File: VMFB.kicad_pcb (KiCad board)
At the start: 2 copper layers, 154.1 x 111.9 mm, 137 parts, among them J1 Screw_Terminal_01x02, J10 Conn_01x03_Pin, J11 Conn_01x08_Pin, J12 Conn_01x06_Pin, J13 Conn_01x03_Pin, J14 Conn_01x03_Pin, J15 Conn_01x03_Pin, J16 Conn_01x03_Pin, J17 Conn_01x03_Pin, J18 Conn_01x03_Pin, J19 Conn_01x02_Pin, J2 USB_A_Stacked, J20 Conn_01x03_Pin, J21 Conn_01x02_Pin, J3 USB_B, J4 Barrel_Jack_Switch, J5 Conn_01x02_Pin, J6 Conn_01x03_Pin, J7 Conn_01x02_Pin, J8 Conn_01x03_Pin, J9 Conn_01x03_Pin, Q1 BC547B, Q2 TIP41C, Q3 BC547B, Q4 BC547B, Q5 BD139, Q6 BC547B, Q7 BC547B, Q8 BC547, U1 NE555P, U2 NE555P, U3 LM358, U4 NE555P, U5 NE555P

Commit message: schemati and pcb tweaking
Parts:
- moved J21 1.52 mm to (217.9, 133.1)
- moved C11 0.48 mm to (162.7, 48.4)
- moved D6 0.48 mm to (183.0, 61.8)
- moved R28 0.48 mm to (177.7, 61.2)
- moved R31 0.48 mm to (182.8, 42.8)
- moved R32 0.48 mm to (187.6, 50.0)
- moved R33 0.48 mm to (186.5, 57.1)
- moved U5 0.48 mm to (182.6, 48.3)
- moved Q6 0.48 mm to (180.2, 65.6)
- moved R23 0.48 mm to (169.5, 68.8)
- moved C13 0.48 mm to (174.9, 59.7)
- moved D4 0.48 mm to (172.1, 45.3)
- moved D7 0.48 mm to (188.4, 45.3)
- moved R27 0.48 mm to (177.5, 42.8)
- moved C14 0.48 mm to (185.8, 66.6)
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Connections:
- J18 pad 2: GND -> IR GND
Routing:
- net IR GND: track 145.5 -> 178.0 mm
- net Net-(D1-K): track 153.8 -> 138.2 mm
- net IR CON/MON: track 100.8 -> 115.0 mm
- net EMPTY MON: track 87.1 -> 100.3 mm
- net DISPENSE CON/MON: track 69.8 -> 59.5 mm, vias 0 -> 1
- net Net-(J17-Pin_1): track 67.6 -> 58.3 mm
- net VCC: track 407.2 -> 416.5 mm
- net PIR MON: track 162.2 -> 154.7 mm
- net Net-(Q2-B): track 24.7 -> 18.9 mm
- net Net-(J8-Pin_1): track 129.8 -> 134.3 mm
- net DISPENSE ADJ: track 16.5 -> 13.6 mm
- net Net-(IR3-A): track 60.8 -> 63.6 mm
- net MOTOR RESET: track 173.4 -> 175.5 mm
- net Net-(J13-Pin_2): track 51.3 -> 49.4 mm
- net GND: track 535.9 -> 534.0 mm
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
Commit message: schemati and pcb tweaking
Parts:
- renumbered J7 to J6, J6 to J7, Q2 to Q1, Q1 to Q2, R11 to R10, R9 to R11, R25 to R23, R23 to R25, R30 to R29, R29 to R30, R33 to R32, R32 to R33, R5 to R4, R4 to R5, R7 to R6, R6 to R7, R10 to R8, R8 to R9
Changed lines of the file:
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@@
     (property "ki_keywords" "connector")
     (attr through_hole)
-    (fp_text reference "J6" (at 0 -2.33 -90) (layer "F.SilkS")
+    (fp_text reference "J7" (at 0 -2.33 -90) (layer "F.SilkS")
         (effects (font (size 1 1) (thickness 0.15)))
     )
@@
     (property "ki_keywords" "R res resistor")
     (attr through_hole)
-    (fp_text reference "R10" (at 1.27 -2.37 90) (layer "F.SilkS")
+    (fp_text reference "R8" (at 1.27 -2.37 90) (layer "F.SilkS")
         (effects (font (size 1 1) (thickness 0.15)))
     )
@@
     (property "ki_keywords" "power NPN Transistor")
     (attr through_hole)
-    (fp_text reference "Q2" (at 2.54 -4.27 90) (layer "F.SilkS")
+    (fp_text reference "Q1" (at 2.54 -4.27 90) (layer "F.SilkS")
         (effects (font (size 1 1) (thickness 0.15)))
     )
@@
     (property "ki_keywords" "R res resistor")
     (attr through_hole)
-    (fp_text reference "R30" (at 4.4698 -0.0612 90) (layer "F.SilkS")
+    (fp_text reference "R29" (at 4.4698 -0.0612 90) (layer "F.SilkS")
         (effects (font (size 1 1) (thickness 0.15)))
     )
@@
     (property "ki_keywords" "R res resistor")
     (attr through_hole)
-    (fp_text reference "R23" (at 1.299 2.54) (layer "F.SilkS")
+    (fp_text reference "R25" (at 1.299 2.54) (layer "F.SilkS")
         (effects (font (size 1 1) (thickness 0.15)))
     )
@@
     (property "ki_keywords" "R res resistor")
     (attr through_hole)
-    (fp_text reference "R25" (at 1.27 -2.72 -90) (layer "F.SilkS")
+    (fp_text reference "R23" (at 1.27 -2.72 -90) (layer "F.SilkS")
         (effects (font (size 1 1) (thickness 0.15)))
     )
@@
     (property "ki_keywords" "connector")
     (attr through_hole)
-    (fp_text reference "J7" (at 0 -2.33) (layer "F.SilkS")
+    (fp_text reference "J6" (at 0 -2.33) (layer "F.SilkS")
         (effects (font (size 1 1) (thickness 0.15)))
     )
@@
     (property "ki_keywords" "R res resistor")
     (attr through_hole)
-    (fp_text reference "R29" (at 4.2164 -0.0254) (layer "F.SilkS")
+    (fp_text reference "R30" (at 4.2164 -0.0254) (layer "F.SilkS")
         (effects (font (size 1 1) (thickness 0.15)))
     )
@@
     (property "ki_keywords" "NPN Transistor")
     (attr through_hole)
-    (fp_text reference "Q1" (at 2.54 -3.56 -90) (layer "F.SilkS")
+    (fp_text reference "Q2" (at 2.54 -3.56 -90) (layer "F.SilkS")
         (effects (font (size 1 1) (thickness 0.15)))
     )
@@
     (property "ki_keywords" "R res resistor")
     (attr through_hole)
-    (fp_text reference "R33" (at 1.27 2.54 90) (layer "F.SilkS")
+    (fp_text reference "R32" (at 1.27 2.54 90) (layer "F.SilkS")
         (effects (font (size 1 1) (thickness 0.15)))
     )
@@
     (property "ki_keywords" "R res resistor")
     (attr through_hole)
-    (fp_text reference "R9" (at 1.27 -2.37 90) (layer "F.SilkS")
+    (fp_text reference "R11" (at 1.27 -2.37 90) (layer "F.SilkS")
         (effects (font (size 1 1) (thickness 0.15)))
     )
@@
     (property "ki_keywords" "R res resistor")
     (attr through_hole)
-    (fp_text reference "R4" (at 1.27 -2.37 90) (layer "F.SilkS")
+    (fp_text reference "R5" (at 1.27 -2.37 90) (layer "F.SilkS")
         (effects (font (size 1 1) (thickness 0.15)))
     )
@@
     (property "ki_keywords" "R res resistor")
     (attr through_hole)
-    (fp_text reference "R5" (at 1.27 -2.37 90) (layer "F.SilkS")
+    (fp_text reference "R4" (at 1.27 -2.37 90) (layer "F.SilkS")
         (effects (font (size 1 1) (thickness 0.15)))
     )
@@
     (property "ki_keywords" "R res resistor")
     (attr through_hole)
-    (fp_text reference "R32" (at 1.328 2.54) (layer "F.SilkS")
+    (fp_text reference "R33" (at 1.328 2.54) (layer "F.SilkS")
         (effects (font (size 1 1) (thickness 0.15)))
     )
@@
     (property "ki_keywords" "R res resistor")
     (attr through_hole)
-    (fp_text reference "R11" (at 1.27 -2.37 90) (layer "F.SilkS")
+    (fp_text reference "R10" (at 1.27 -2.37 90) (layer "F.SilkS")
         (effects (font (size 1 1) (thickness 0.15)))
     )
@@
     (property "ki_keywords" "R res resistor")
     (attr through_hole)
-    (fp_text reference "R8" (at 4.709 0.0826 90) (layer "F.SilkS")
+    (fp_text reference "R9" (at 4.709 0.0826 90) (layer "F.SilkS")
         (effects (font (size 1 1) (thickness 0.15)))
     )
@@
     (property "ki_keywords" "R res resistor")
     (attr through_hole)
-    (fp_text reference "R6" (at 1.27 -2.72 90) (layer "F.SilkS")
+    (fp_text reference "R7" (at 1.27 -2.72 90) (layer "F.SilkS")
         (effects (font (size 1 1) (thickness 0.15)))
     )
@@
     (property "ki_keywords" "R res resistor")
     (attr through_hole)
-    (fp_text reference "R7" (at 1.27 -2.72 90) (layer "F.SilkS")
+    (fp_text reference "R6" (at 1.27 -2.72 90) (layer "F.SilkS")
         (effects (font (size 1 1) (thickness 0.15)))
     )
@@
       (xy 90.17 76.708)
       (xy 90.17 53.34)
-      (xy 93.98 53.086)
-      (xy 98.298 58.42)
+      (xy 93.726 52.07)
+      (xy 98.298 60.96)
       (xy 98.293338 77.560157)
     )
@@
       (xy 96.012 39.624)
       (xy 96.012 47.752)
-      (xy 93.98 53.086)
+      (xy 93.726 52.07)
     )
     (stroke (width 0.1) (type solid)) (fill none) (layer "F.SilkS"))
@@
       (xy 96.012 39.624)
       (xy 96.012 47.752)
-      (xy 93.98 53.086)
-      (xy 98.298 58.42)
+      (xy 93.726 52.07)
+      (xy 98.298 60.96)
       (xy 98.293338 77.560157)
       (xy 126.492 80.518)

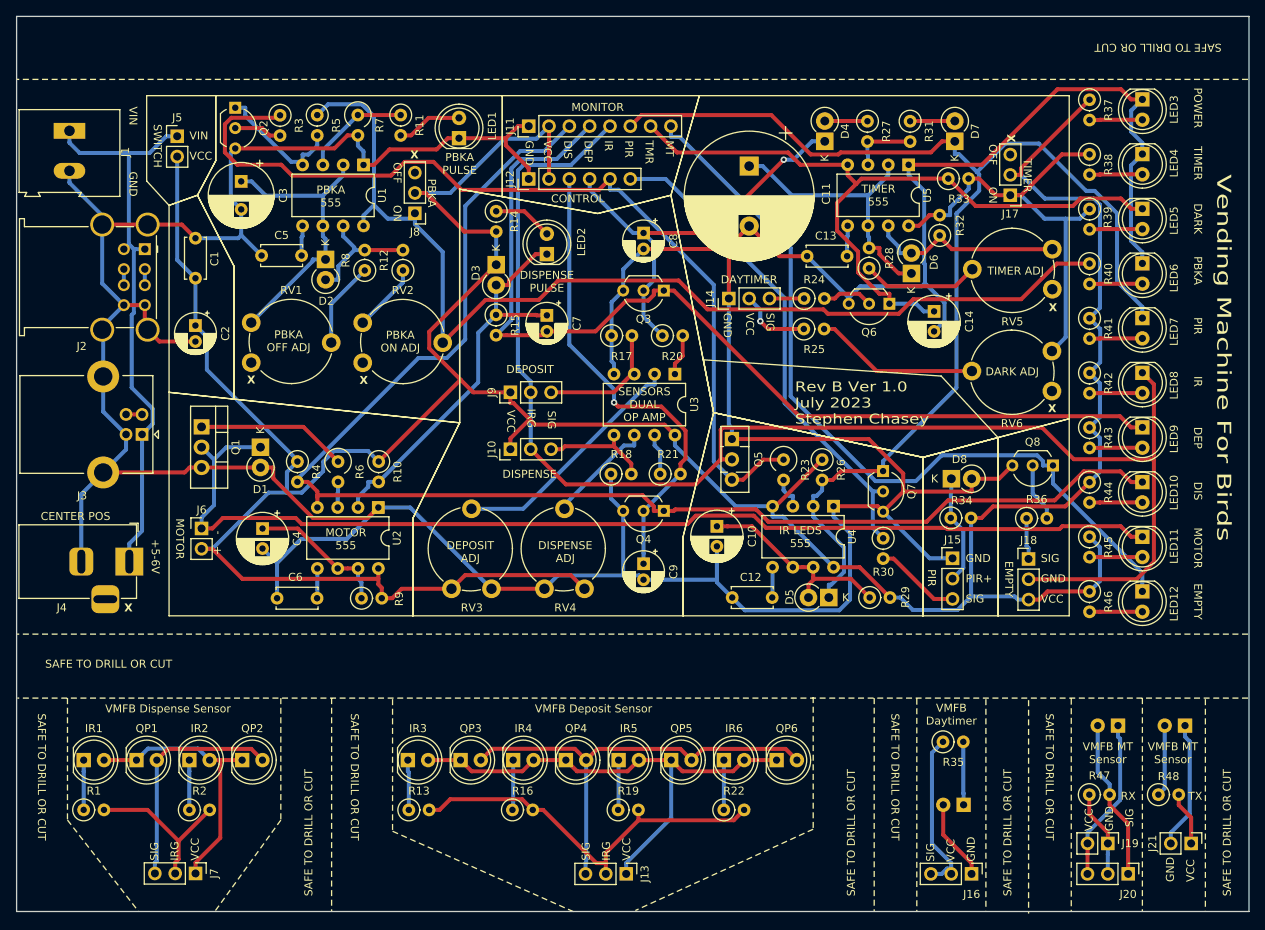
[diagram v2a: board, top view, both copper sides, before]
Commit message: schematic and pcb tweaking
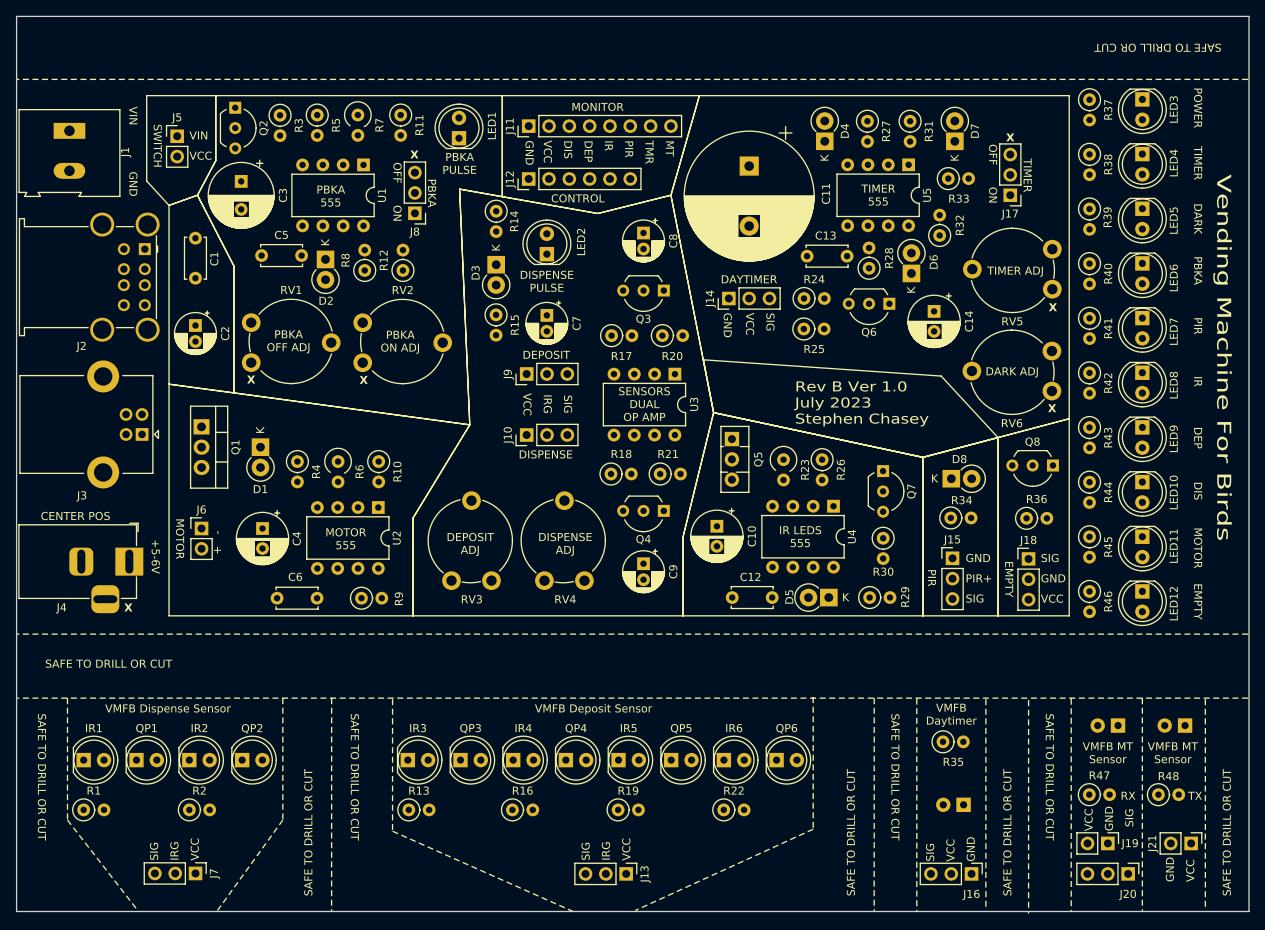
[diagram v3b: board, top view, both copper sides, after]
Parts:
- R33: value 47K -> 10K
- moved J9 3.06 mm to (134.9, 74.4)
- moved J10 2.70 mm to (134.9, 82.0)
- moved RV3 1.02 mm to (130.5, 100.2)
- moved RV4 1.02 mm to (142.1, 100.2)
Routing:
- net GND: track 534.0 -> 0.00 mm
- net VCC: track 416.5 -> 0.00 mm
- net IR GND: track 178.0 -> 0.00 mm
- net MOTOR RESET: track 175.5 -> 0.00 mm
- net PIR MON: track 154.7 -> 0.00 mm
- net Net-(D1-K): track 138.2 -> 0.00 mm
- net Net-(J8-Pin_1): track 134.3 -> 0.00 mm
- net DEPOSIT MON: track 124.1 -> 0.00 mm
- net IR CON/MON: track 115.0 -> 0.00 mm
- net EMPTY MON: track 100.3 -> 0.00 mm
- net TIMER MON: track 93.2 -> 0.00 mm
- net Net-(J1-Pin_1): track 72.4 -> 0.00 mm
- net Net-(IR3-A): track 63.6 -> 0.00 mm
- net PIR CON/MON: track 61.9 -> 0.00 mm
- net DISPENSE CON/MON: track 59.5 -> 0.00 mm, vias 1 -> 0
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
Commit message: schematic and pcb tweaking
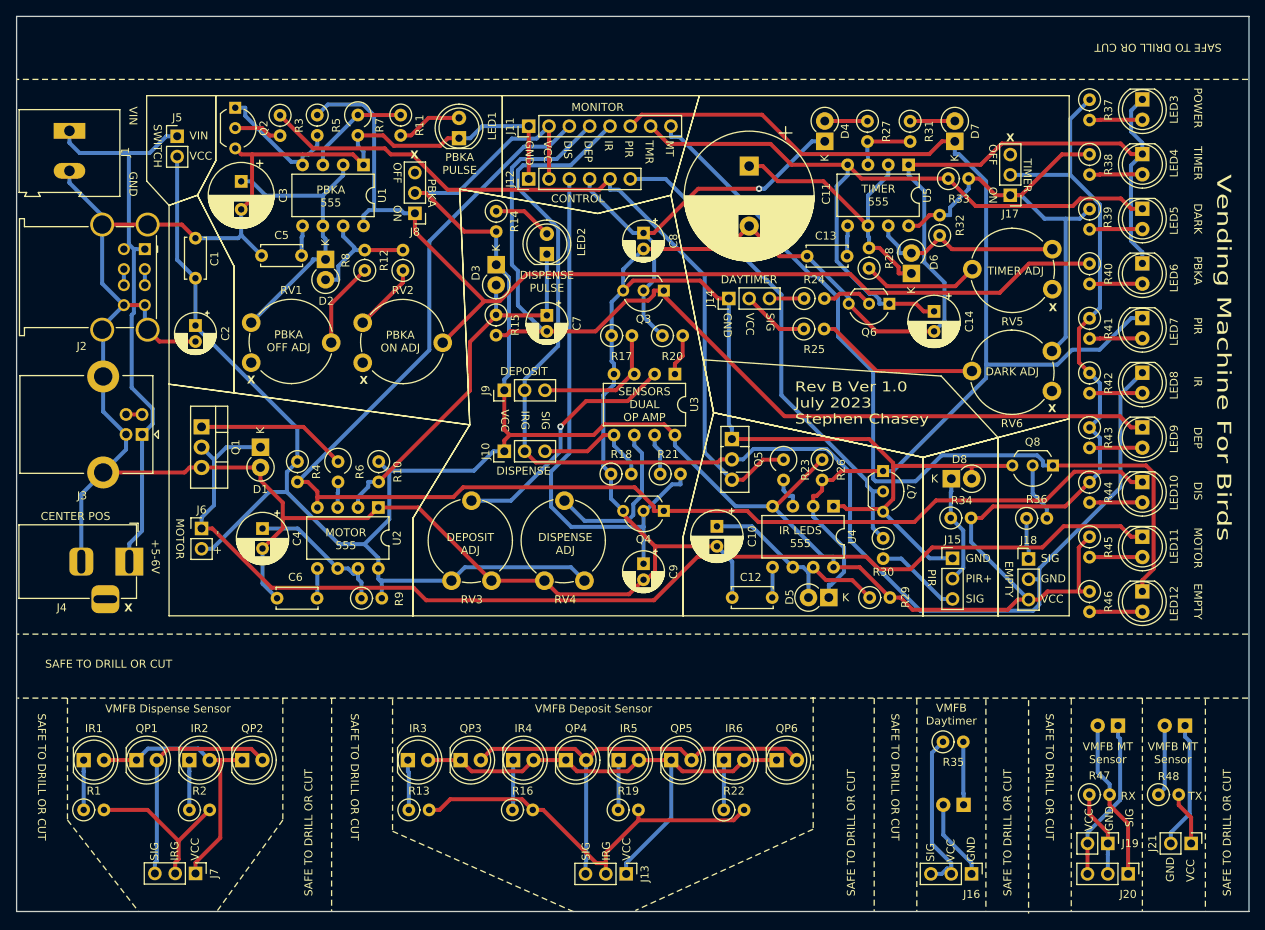
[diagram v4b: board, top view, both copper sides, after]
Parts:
- moved J10 3.45 mm to (132.1, 84.1)
- moved J9 3.45 mm to (132.1, 76.5)
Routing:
- net GND: track 0.00 -> 518.5 mm
- net VCC: track 0.00 -> 397.3 mm
- net MOTOR RESET: track 0.00 -> 174.3 mm
- net IR GND: track 0.00 -> 167.7 mm
- net Net-(D1-K): track 0.00 -> 144.9 mm
- net PIR MON: track 0.00 -> 141.1 mm
- net Net-(J8-Pin_1): track 0.00 -> 129.7 mm
- net DEPOSIT MON: track 0.00 -> 125.5 mm
- net EMPTY MON: track 0.00 -> 108.7 mm
- net IR CON/MON: track 0.00 -> 97.7 mm
- net TIMER MON: track 0.00 -> 94.2 mm
- net Net-(J1-Pin_1): track 0.00 -> 72.4 mm
- net DISPENSE CON/MON: track 0.00 -> 68.9 mm
- net Net-(IR3-A): track 0.00 -> 63.6 mm
- net PIR CON/MON: track 0.00 -> 61.9 mm
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
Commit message: removed 10K resistor to ground fromo empty sensor
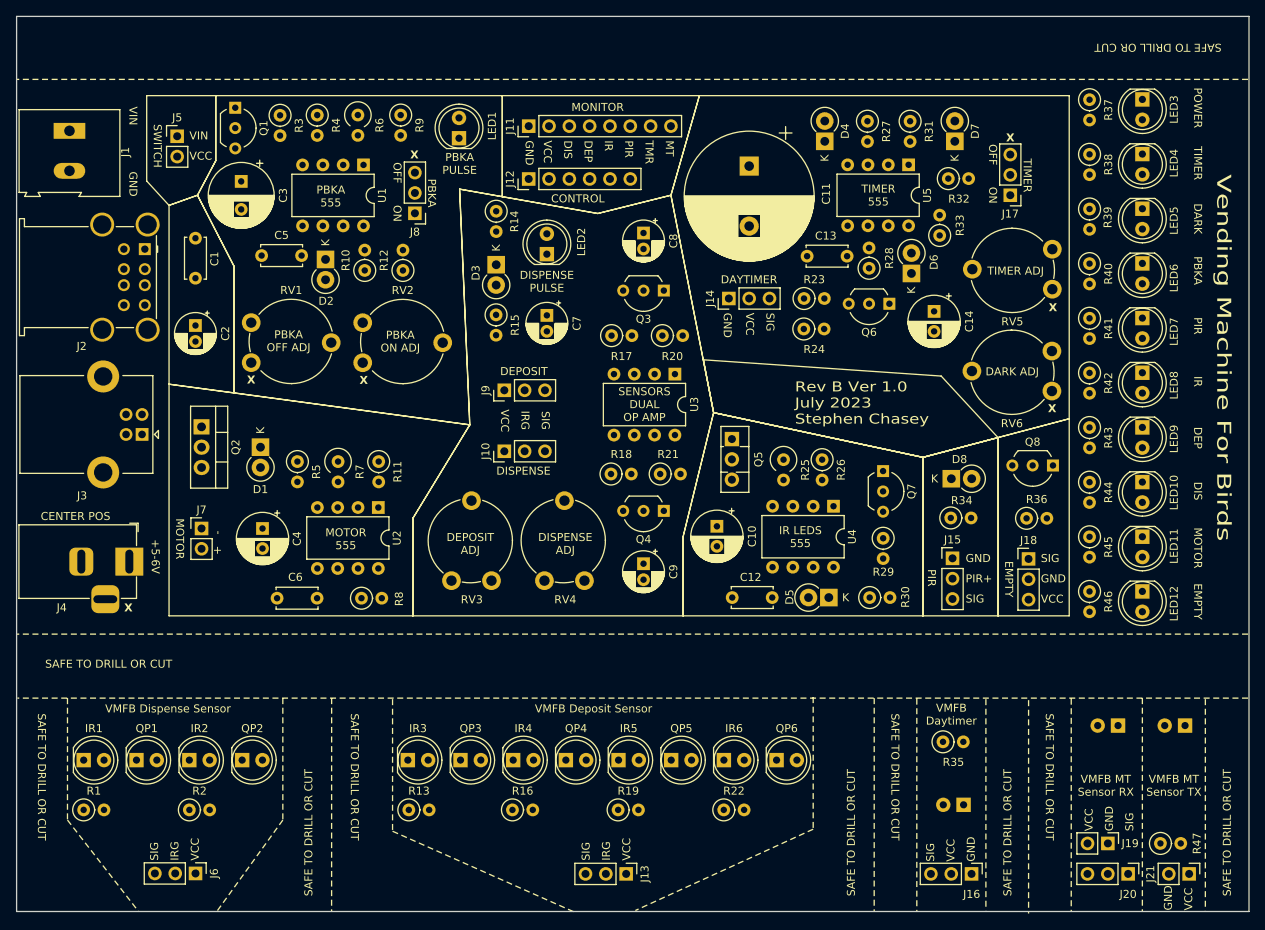
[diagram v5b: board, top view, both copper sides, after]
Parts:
- removed the R47 at (205.2, 127.0)
- moved R47 6.10 mm to (214.1, 133.1)
- moved J21 3.82 mm to (217.7, 136.9)
- renumbered J7 to J6, J6 to J7, Q2 to Q1, Q1 to Q2, R8 to R10, R10 to R11, R24 to R23, R25 to R24, R23 to R25, R30 to R29, R29 to R30, R33 to R32, R32 to R33, R5 to R4, R48 to R47, R4 to R5, R7 to R6, R6 to R7, R9 to R8, R11 to R9
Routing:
- net GND: track 518.5 -> 0.00 mm
- net VCC: track 397.3 -> 0.00 mm
- net MOTOR RESET: track 174.3 -> 0.00 mm
- net IR GND: track 167.7 -> 0.00 mm
- net Net-(D1-K): track 144.9 -> 0.00 mm
- net PIR MON: track 141.1 -> 0.00 mm
- net Net-(J8-Pin_1): track 129.7 -> 0.00 mm
- net DEPOSIT MON: track 125.5 -> 0.00 mm
- net EMPTY MON: track 108.7 -> 0.00 mm
- net IR CON/MON: track 97.7 -> 0.00 mm
- net TIMER MON: track 94.2 -> 0.00 mm
- net Net-(J1-Pin_1): track 72.4 -> 0.00 mm
- net DISPENSE CON/MON: track 68.9 -> 0.00 mm
- net Net-(IR3-A): track 63.6 -> 0.00 mm
- net PIR CON/MON: track 61.9 -> 0.00 mm
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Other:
- board text added: "VMFB MT Sensor RX"
- board text added: "VMFB MT Sensor TX"
- board text removed: "RX"
- board text removed: "TX"
- board text removed: "VMFB MT Sensor"
